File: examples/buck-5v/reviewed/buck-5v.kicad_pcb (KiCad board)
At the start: 2 copper layers, 126 x 56 mm, 11 parts, among them J1 12V IN, J2 5V OUT, U1 LM2596S-5

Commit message: Measure the copper that goes out and comes back, and the text drawn on text
The reviewer sent screenshots with circles on them. Two kinds: strings
printed through each other on the schematics, and copper that leaves a
pad, travels three sides of a rectangle and arrives four millimetres
away. Neither had a rule that could see it - `text_over_wire` measured
text against nets and nothing measured text against text, and
`route.detour` weighs a whole net, which averages one bad connection
away under any ratio worth setting.

New rule `route.wander`: one continuous run of copper - pad or junction
at each end - against the shortest way between those two ends that
clears the packages in between. The baseline walks the perimeter of
whatever the straight line crosses, so an opamp's feedback wrap is
measured against going round the package rather than through it. On
KiCad's 18 demo boards it fires once at the shipped 2.0x.

`readability.text_over_text` and `_over_wire` are regraded info: they
fire on 14 and 10 of those 18 human sheets. That is the estimate
talking, not the drawing. `ai-generated` still promotes both to errors,
so every generated design has to have none - and the five examples do.

What the two rules then made us fix:

* a net label's anchor cannot move, but its reading direction can. Each
  name is now offered the four quarters of its anchor and takes the
  first that prints over nothing. Power symbol names and PWR_FLAG names
  get the same treatment - four grounds on one row printed GNGNGNGND.
  Schematic text overlaps: buck 1, motor 2, carrier 1, fpga 7, all to 0.
* a plane crossing was priced at forty times front copper per
  millimetre, which is a prohibition, not a price: one millimetre of
  crossing bought a forty millimetre tour and the boards had grown
  them. Thirty is where neither `route.wander` nor `route.return_path`
  fires. Buck, motor and carrier now have no wander findings.
* `write_variant` resolves the routes a second time, so the
  straight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
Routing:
- net /+5V: track 141.9 -> 131.6 mm
- net /+12V: track 61.9 -> 58.1 mm
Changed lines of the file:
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@@
 	(gr_line (start 226.0 116.0) (end 100.0 116.0) (stroke (width 0.1) (type default)) (layer "Edge.Cuts"))
 	(gr_line (start 100.0 116.0) (end 100.0 60.0) (stroke (width 0.1) (type default)) (layer "Edge.Cuts"))
-	(segment (start 110.0 72.0) (end 110.0 65.5) (width 1.0) (layer "F.Cu") (net 2))
-	(segment (start 110.0 65.5) (end 111.5 64.0) (width 1.0) (layer "F.Cu") (net 2))
-	(segment (start 111.5 64.0) (end 128.3 64.0) (width 1.0) (layer "F.Cu") (net 2))
+	(segment (start 110.0 72.0) (end 120.3 72.0) (width 1.0) (layer "F.Cu") (net 2))
+	(segment (start 120.3 72.0) (end 128.3 64.0) (width 1.0) (layer "F.Cu") (net 2))
 	(segment (start 128.3 64.0) (end 128.3 72.0) (width 1.0) (layer "F.Cu") (net 2))
 	(segment (start 128.3 64.0) (end 145.5 64.0) (width 1.0) (layer "F.Cu") (net 2))
@@
 	(segment (start 190.55 90.0) (end 196.3 90.0) (width 1.0) (layer "F.Cu") (net 3))
 	(segment (start 196.3 90.0) (end 196.3 96.0) (width 1.0) (layer "F.Cu") (net 3))
-	(segment (start 196.3 90.0) (end 205.5 90.0) (width 1.0) (layer "F.Cu") (net 3))
-	(segment (start 205.5 90.0) (end 207.0 91.5) (width 1.0) (layer "F.Cu") (net 3))
-	(segment (start 207.0 91.5) (end 207.0 100.5) (width 1.0) (layer "F.Cu") (net 3))
-	(segment (start 207.0 100.5) (end 208.5 102.0) (width 1.0) (layer "F.Cu") (net 3))
-	(segment (start 208.5 102.0) (end 210.0 102.0) (width 1.0) (layer "F.Cu") (net 3))
-	(segment (start 210.0 102.0) (end 216.0 96.0) (width 1.0) (layer "F.Cu") (net 3))
-	(segment (start 196.3 96.0) (end 196.3 100.606) (width 0.4) (layer "F.Cu") (net 3))
-	(segment (start 196.3 100.606) (end 197.694 102.0) (width 0.4) (layer "F.Cu") (net 3))
-	(segment (start 197.694 102.0) (end 199.088 103.394) (width 0.4) (layer "F.Cu") (net 3))
-	(segment (start 199.088 103.394) (end 199.0875 106.0) (width 0.4) (layer "F.Cu") (net 3))
+	(segment (start 196.3 90.0) (end 210.0 90.0) (width 1.0) (layer "F.Cu") (net 3))
+	(segment (start 210.0 90.0) (end 216.0 96.0) (width 1.0) (layer "F.Cu") (net 3))
+	(segment (start 196.3 96.0) (end 196.3 103.2125) (width 0.4) (layer "F.Cu") (net 3))
+	(segment (start 196.3 103.2125) (end 199.0875 106.0) (width 0.4) (layer "F.Cu") (net 3))
 	(segment (start 200.9125 106.0) (end 206.0625 106.0) (width 0.4) (layer "F.Cu") (net 4))
 	(segment (start 110.0 77.0) (end 110.0 108.5) (width 1.0) (layer "F.Cu") (net 1))
@@
 	(via (at 103.5 63.5) (size 0.8) (drill 0.4) (layers "F.Cu" "B.Cu") (net 1))
 	(via (at 103.5 112.5) (size 0.8) (drill 0.4) (layers "F.Cu" "B.Cu") (net 1))
+	(via (at 113.5 63.5) (size 0.8) (drill 0.4) (layers "F.Cu" "B.Cu") (net 1))
 	(via (at 113.5 112.5) (size 0.8) (drill 0.4) (layers "F.Cu" "B.Cu") (net 1))
+	(via (at 123.5 63.5) (size 0.8) (drill 0.4) (layers "F.Cu" "B.Cu") (net 1))
 	(via (at 123.5 112.5) (size 0.8) (drill 0.4) (layers "F.Cu" "B.Cu") (net 1))
 	(via (at 133.5 112.5) (size 0.8) (drill 0.4) (layers "F.Cu" "B.Cu") (net 1))
@@
 	(via (at 112.5 69.5) (size 0.8) (drill 0.4) (layers "F.Cu" "B.Cu") (net 1))
 	(via (at 118.5 69.5) (size 0.8) (drill 0.4) (layers "F.Cu" "B.Cu") (net 1))
-	(via (at 124.5 69.5) (size 0.8) (drill 0.4) (layers "F.Cu" "B.Cu") (net 1))
 	(via (at 130.5 69.5) (size 0.8) (drill 0.4) (layers "F.Cu" "B.Cu") (net 1))
 	(via (at 136.5 69.5) (size 0.8) (drill 0.4) (layers "F.Cu" "B.Cu") (net 1))
@@
 	(via (at 202.5 93.5) (size 0.8) (drill 0.4) (layers "F.Cu" "B.Cu") (net 1))
 	(via (at 208.5 93.5) (size 0.8) (drill 0.4) (layers "F.Cu" "B.Cu") (net 1))
-	(via (at 214.5 93.5) (size 0.8) (drill 0.4) (layers "F.Cu" "B.Cu") (net 1))
 	(via (at 220.5 93.5) (size 0.8) (drill 0.4) (layers "F.Cu" "B.Cu") (net 1))
 	(via (at 106.5 99.5) (size 0.8) (drill 0.4) (layers "F.Cu" "B.Cu") (net 1))

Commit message: Stop hiding the hairpins behind the pads they are drawn on
The reviewer said the 135 degree bends and the odd-angle runs were still
there. They were. `route.acute_angle` skipped any corner within a pad's
*radius*, and a 0805's radius is 0.47 mm, which covers the five or six
ordinary corners a chamfered pad entry leaves inside it. Eleven of the
thirteen hairpins on these five boards sat in that shadow, because a pad
is exactly where a route that has to double back does it.

The exemption is the pad's connection point now, not a disc around it.
Two branches leaving one pad stay exempt - the pad's own copper fills the
wedge, so it is not an acid trap - but nought degrees never is: that is
one run drawn twice, and no pad excuses it.

Then the generator had to stop making them:

* `_untraced` drops the copper a second run lays on top of the first.
  The shorter is inside the longer and carries nothing it does not; both
  get trimmed, because dropping only the duplicate leaves the other
  hanging over the gap, which is `route.stub`. It runs before the runs
  are joined, while the pair is still two tracks sharing an end - once
  joined, the shared point is usually a pad, and the clean-up passes pin
  those precisely so they cannot take copper off them.
* `_straighten` only takes the direct line when it lands on the 45 grid.
  Between two pads at whatever coordinates their packages give them it
  usually does not: last round it made a nine millimetre run at 169.7
  degrees, which is the slip-of-the-mouse angle `route.odd_angle` is for.

Measured across the five boards: off-grid segments 1 to 0, 180 degree
reversals 6 to 0, and the motor board's `route.return_path` finding went
with the 11 mm of copper it was measuring.

Three corners survive, all on the FPGA board, all where a knee lands a
fraction past where its own two legs cross - legs of 0.07 and 0.25 mm on
two, 0.15 and 0.5 mm on the third. Refusing a knee that short is worse:
the segment then keeps the angle it had, a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
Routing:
- net /+5V: track 131.6 -> 141.9 mm
- net /+12V: track 58.1 -> 61.9 mm
- net GND: vias 194 -> 193
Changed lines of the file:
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@@
 	(gr_line (start 226.0 116.0) (end 100.0 116.0) (stroke (width 0.1) (type default)) (layer "Edge.Cuts"))
 	(gr_line (start 100.0 116.0) (end 100.0 60.0) (stroke (width 0.1) (type default)) (layer "Edge.Cuts"))
-	(segment (start 110.0 72.0) (end 120.3 72.0) (width 1.0) (layer "F.Cu") (net 2))
-	(segment (start 120.3 72.0) (end 128.3 64.0) (width 1.0) (layer "F.Cu") (net 2))
+	(segment (start 110.0 72.0) (end 110.0 65.5) (width 1.0) (layer "F.Cu") (net 2))
+	(segment (start 110.0 65.5) (end 111.5 64.0) (width 1.0) (layer "F.Cu") (net 2))
+	(segment (start 111.5 64.0) (end 128.3 64.0) (width 1.0) (layer "F.Cu") (net 2))
 	(segment (start 128.3 64.0) (end 128.3 72.0) (width 1.0) (layer "F.Cu") (net 2))
 	(segment (start 128.3 64.0) (end 145.5 64.0) (width 1.0) (layer "F.Cu") (net 2))
@@
 	(segment (start 190.55 90.0) (end 196.3 90.0) (width 1.0) (layer "F.Cu") (net 3))
 	(segment (start 196.3 90.0) (end 196.3 96.0) (width 1.0) (layer "F.Cu") (net 3))
-	(segment (start 196.3 90.0) (end 210.0 90.0) (width 1.0) (layer "F.Cu") (net 3))
-	(segment (start 210.0 90.0) (end 216.0 96.0) (width 1.0) (layer "F.Cu") (net 3))
-	(segment (start 196.3 96.0) (end 196.3 103.2125) (width 0.4) (layer "F.Cu") (net 3))
-	(segment (start 196.3 103.2125) (end 199.0875 106.0) (width 0.4) (layer "F.Cu") (net 3))
+	(segment (start 196.3 90.0) (end 205.5 90.0) (width 1.0) (layer "F.Cu") (net 3))
+	(segment (start 205.5 90.0) (end 207.0 91.5) (width 1.0) (layer "F.Cu") (net 3))
+	(segment (start 207.0 91.5) (end 207.0 100.5) (width 1.0) (layer "F.Cu") (net 3))
+	(segment (start 207.0 100.5) (end 208.5 102.0) (width 1.0) (layer "F.Cu") (net 3))
+	(segment (start 208.5 102.0) (end 210.0 102.0) (width 1.0) (layer "F.Cu") (net 3))
+	(segment (start 210.0 102.0) (end 216.0 96.0) (width 1.0) (layer "F.Cu") (net 3))
+	(segment (start 196.3 96.0) (end 196.3 100.606) (width 0.4) (layer "F.Cu") (net 3))
+	(segment (start 196.3 100.606) (end 197.694 102.0) (width 0.4) (layer "F.Cu") (net 3))
+	(segment (start 197.694 102.0) (end 199.088 103.394) (width 0.4) (layer "F.Cu") (net 3))
+	(segment (start 199.088 103.394) (end 199.0875 106.0) (width 0.4) (layer "F.Cu") (net 3))
 	(segment (start 200.9125 106.0) (end 206.0625 106.0) (width 0.4) (layer "F.Cu") (net 4))
 	(segment (start 110.0 77.0) (end 110.0 108.5) (width 1.0) (layer "F.Cu") (net 1))
@@
 	(via (at 103.5 63.5) (size 0.8) (drill 0.4) (layers "F.Cu" "B.Cu") (net 1))
 	(via (at 103.5 112.5) (size 0.8) (drill 0.4) (layers "F.Cu" "B.Cu") (net 1))
-	(via (at 113.5 63.5) (size 0.8) (drill 0.4) (layers "F.Cu" "B.Cu") (net 1))
 	(via (at 113.5 112.5) (size 0.8) (drill 0.4) (layers "F.Cu" "B.Cu") (net 1))
-	(via (at 123.5 63.5) (size 0.8) (drill 0.4) (layers "F.Cu" "B.Cu") (net 1))
 	(via (at 123.5 112.5) (size 0.8) (drill 0.4) (layers "F.Cu" "B.Cu") (net 1))
 	(via (at 133.5 112.5) (size 0.8) (drill 0.4) (layers "F.Cu" "B.Cu") (net 1))
@@
 	(via (at 112.5 69.5) (size 0.8) (drill 0.4) (layers "F.Cu" "B.Cu") (net 1))
 	(via (at 118.5 69.5) (size 0.8) (drill 0.4) (layers "F.Cu" "B.Cu") (net 1))
+	(via (at 124.5 69.5) (size 0.8) (drill 0.4) (layers "F.Cu" "B.Cu") (net 1))
 	(via (at 130.5 69.5) (size 0.8) (drill 0.4) (layers "F.Cu" "B.Cu") (net 1))
 	(via (at 136.5 69.5) (size 0.8) (drill 0.4) (layers "F.Cu" "B.Cu") (net 1))
@@
 	(via (at 202.5 93.5) (size 0.8) (drill 0.4) (layers "F.Cu" "B.Cu") (net 1))
 	(via (at 208.5 93.5) (size 0.8) (drill 0.4) (layers "F.Cu" "B.Cu") (net 1))
+	(via (at 214.5 93.5) (size 0.8) (drill 0.4) (layers "F.Cu" "B.Cu") (net 1))
 	(via (at 220.5 93.5) (size 0.8) (drill 0.4) (layers "F.Cu" "B.Cu") (net 1))
 	(via (at 106.5 99.5) (size 0.8) (drill 0.4) (layers "F.Cu" "B.Cu") (net 1))
@@
 	(via (at 202.5 99.5) (size 0.8) (drill 0.4) (layers "F.Cu" "B.Cu") (net 1))
 	(via (at 208.5 99.5) (size 0.8) (drill 0.4) (layers "F.Cu" "B.Cu") (net 1))
-	(via (at 214.5 99.5) (size 0.8) (drill 0.4) (layers "F.Cu" "B.Cu") (net 1))
 	(via (at 220.5 99.5) (size 0.8) (drill 0.4) (layers "F.Cu" "B.Cu") (net 1))
 	(via (at 106.5 105.5) (size 0.8) (drill 0.4) (layers "F.Cu" "B.Cu") (net 1))

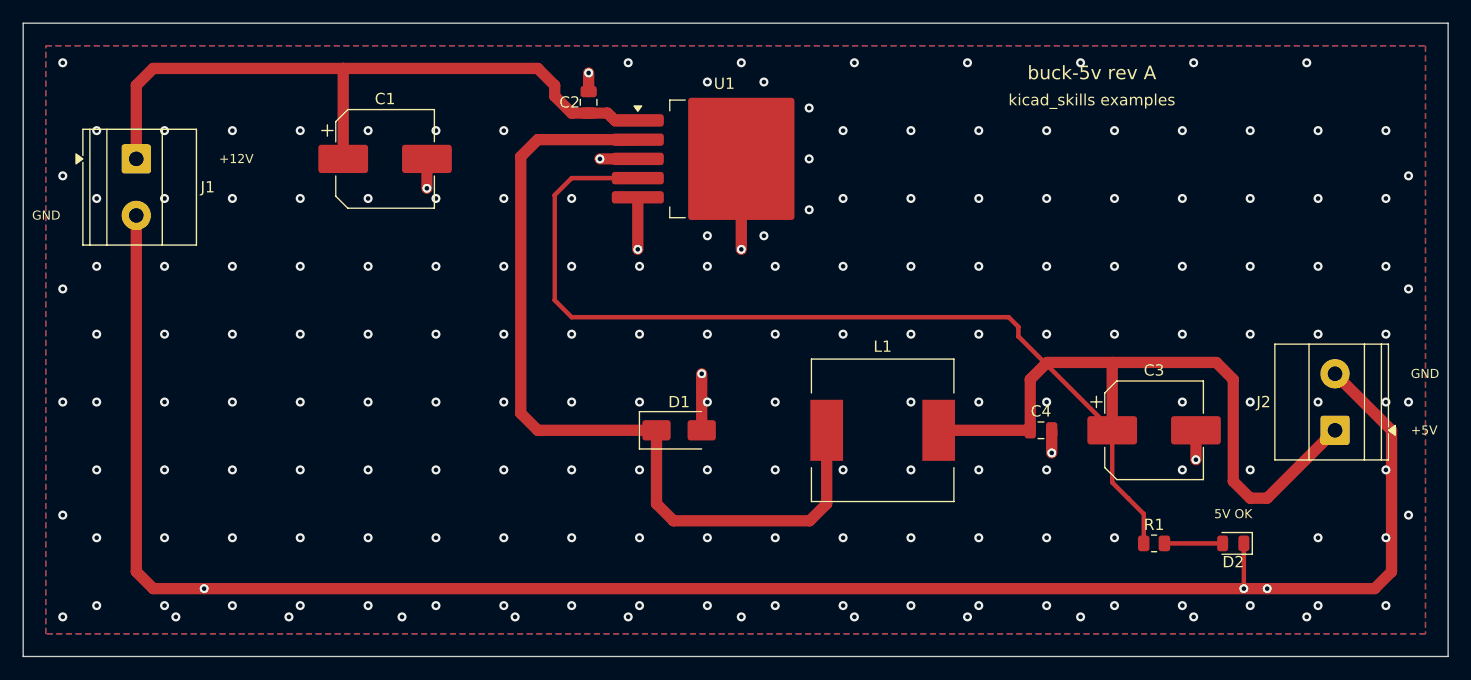
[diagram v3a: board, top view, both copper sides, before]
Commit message: Learn the drawing from the boards people drew
The brief for this round: relying on the autorouter and the numbers alone is
not enough - organise what pictorial correctness looks like from ordinary
circuits and open designs, and improve the drawing itself. So it starts in
KiCad's own demo corpus, measured and looked at, and ends with the habits
pushed into the generator.

tools/board_signature.py (new) reduces "looks autorouted" to five numbers.
Hand-routed two-layer boards cluster tightly: 10-47% of copper on the second
face, median segments 1.8-3.5 mm, 9-25 corners per decimetre, 91-98% of them
45s, 0.3-16 vias per decimetre. Rendering interf_u beside our boards says the
same thing in one glance: a layer has a direction, a bus travels as a bundle,
a person covers an offset with the long straight and one diagonal.

Three habits, now in the generator:

* Router.route(follow=...): cells beside a sibling net's path are discounted,
  so a bus (nets sharing a name prefix - I2S_*, SPI_*) travels as parallel
  lanes in one corridor. The discount is a fraction of a step, so it never
  buys a detour.
* _doglegged: every wiggly stretch is redrawn as the human stroke - the
  straight along the dominant direction plus one 45 - when the dogleg is
  clear, recursing into halves where a crossing blocks the whole. The op-amp
  board's median segment rose from 0.75 mm and its corner rate fell from
  38/dm; the FPGA board landed at 1.54 mm and 17.8/dm, inside the human band.
* Purposeful stitching: the 6 mm via carpet is gone. A ring at the rim, vias
  beside every back-layer crossing (where the plane is actually cut), and a
  coarse 12 mm mesh so no pour orphans. Vias/dm: buck 41 -> 18, carrier
  28 -> 13, all five inside the corpus band, pour_fragmented still silent.

Three failures the round produced and what they taught:

* pinned(): reshaping may not move copper off any point inside an own-net
  pad - the centre alone was not enough, a routed run touches off-centre and
  the ove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
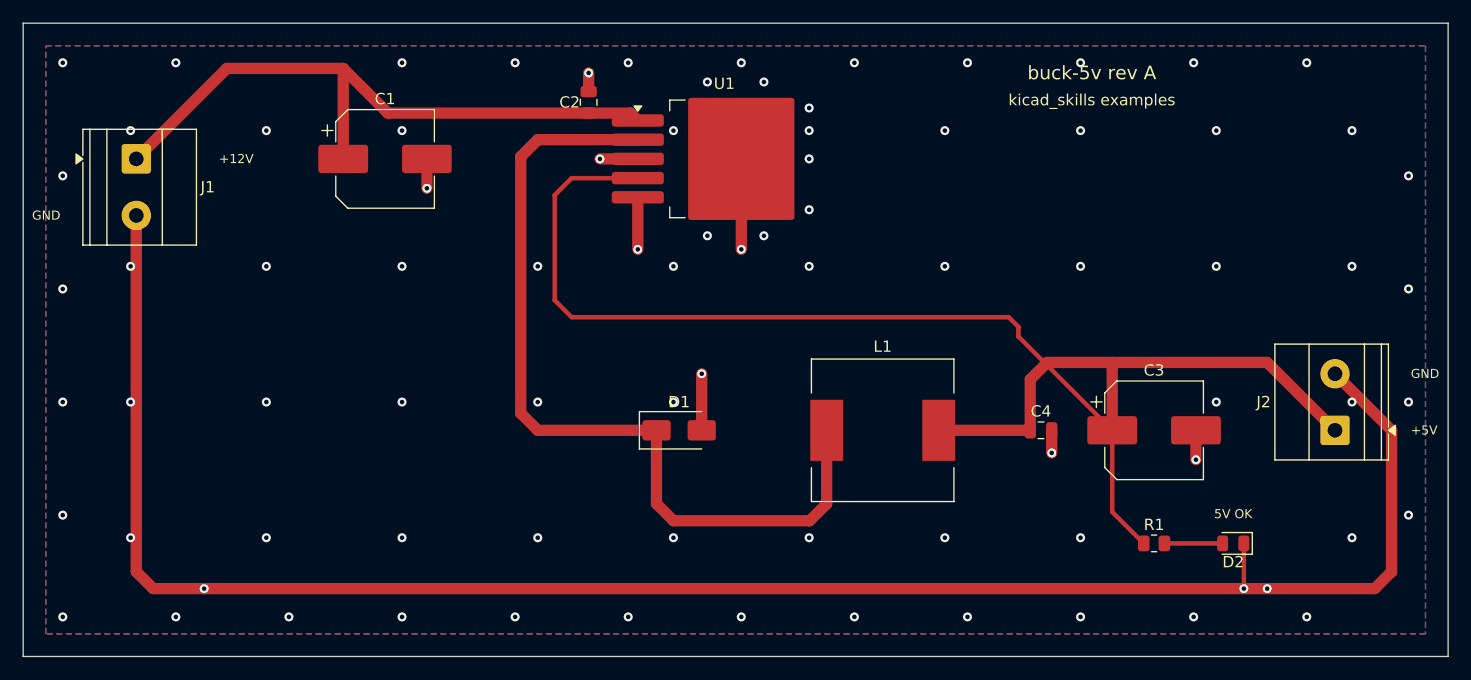
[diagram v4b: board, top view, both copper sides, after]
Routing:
- net /+5V: track 141.9 -> 131.6 mm
- net /+12V: track 61.9 -> 57.6 mm
- net GND: vias 193 -> 84
